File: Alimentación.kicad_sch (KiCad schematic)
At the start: 9 parts, among them J2 Screw_Terminal_01x03, U2 TL074, U3 TL072

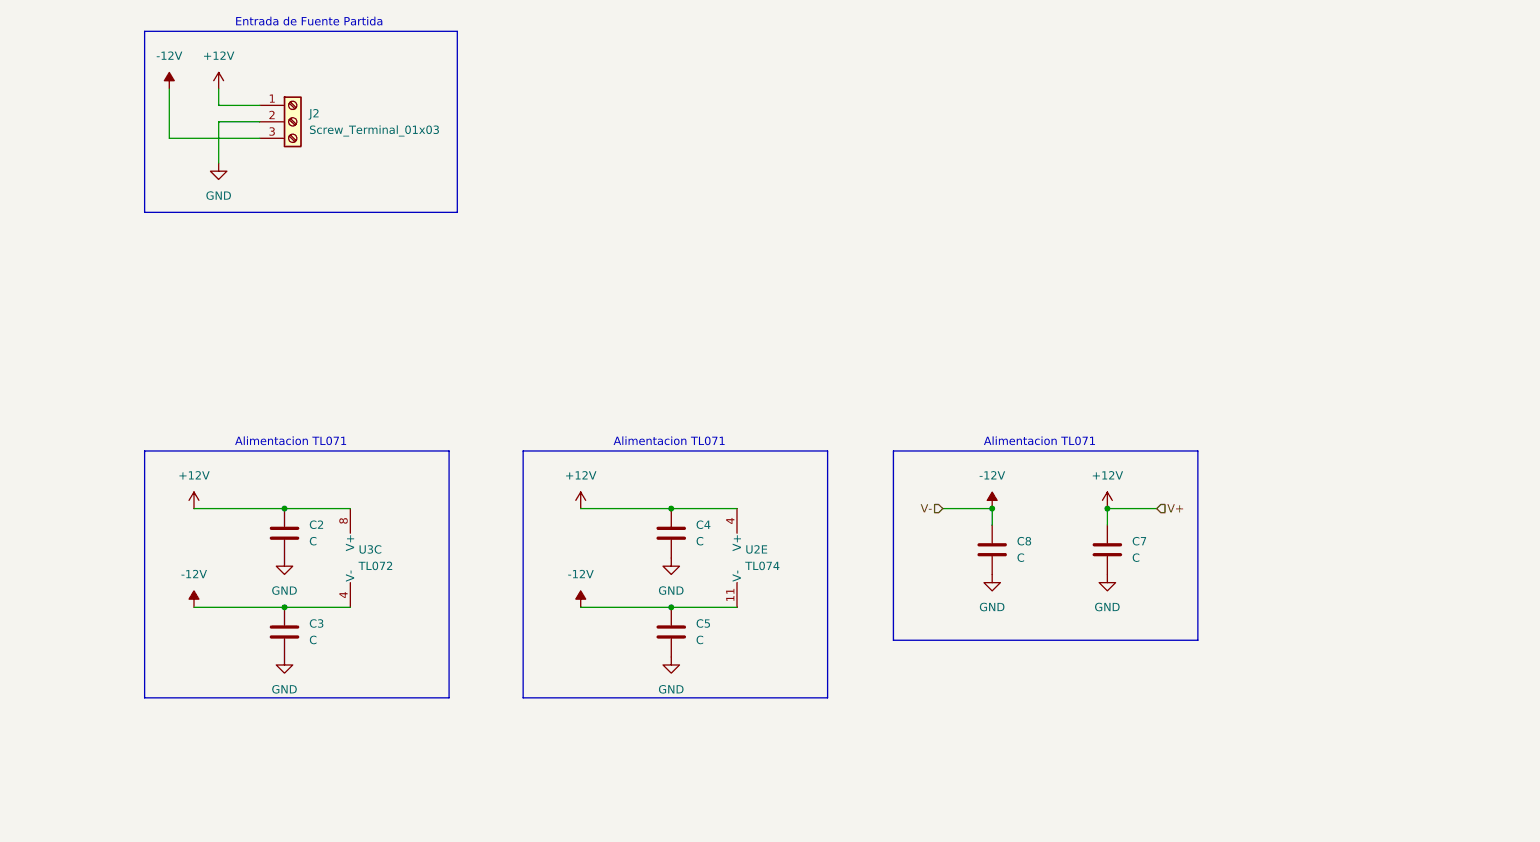
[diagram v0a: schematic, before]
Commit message: Update schematics: signal conditioning, power, ESP32-S3, output, and add signal measurement sub-sheet
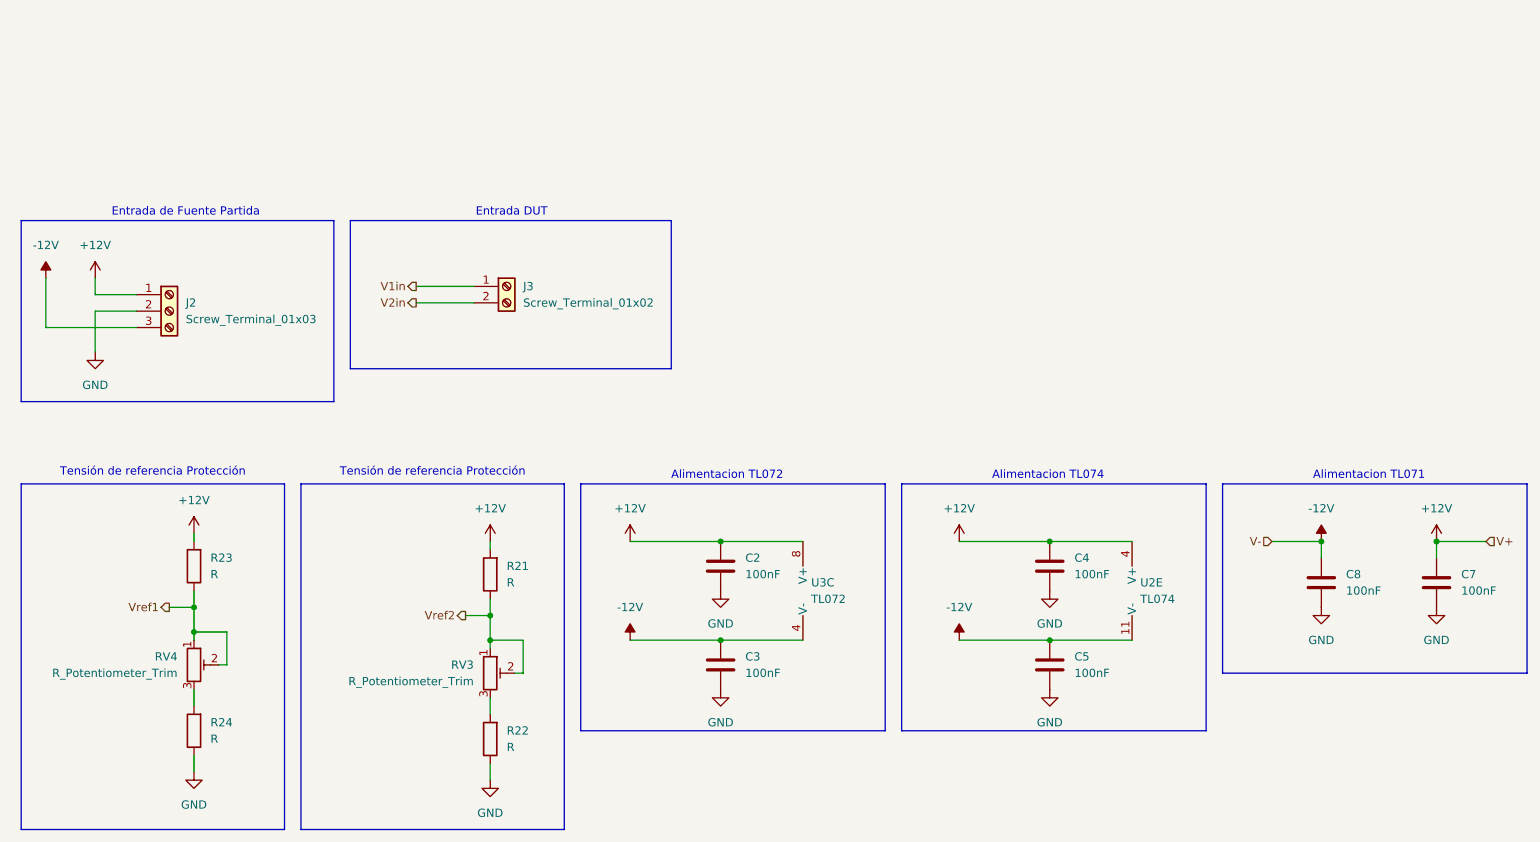
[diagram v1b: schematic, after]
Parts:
- added J3: Screw_Terminal_01x02, TerminalBlock:TerminalBlock_MaiXu_MX126-5.0-02P_1x02_P5.00mm, symbol Connector:Screw_Terminal_01x02
- added R21, R22, R23, R24: R, Resistor_THT:R_Axial_DIN0207_L6.3mm_D2.5mm_P10.16mm_Horizontal, symbol Device:R
- added RV3, RV4: R_Potentiometer_Trim, Potentiometer_THT:Potentiometer_Bourns_3266Y_Vertical, symbol Device:R_Potentiometer_Trim
- C2, C3, C4, C5, C7, C8: value C -> 100nF; footprint (none) -> Capacitor_THT:C_Disc_D7.5mm_W2.5mm_P5.00mm
- J2: footprint (none) -> TerminalBlock:TerminalBlock_MaiXu_MX126-5.0-03P_1x03_P5.00mm
- U2: footprint (none) -> Package_DIP:CERDIP-14_W7.62mm_SideBrazed_LongPads_Socket
- U3: footprint (none) -> Package_DIP:CERDIP-8_W7.62mm_SideBrazed_LongPads_Socket
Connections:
- net +12V: now also R21.2, R23.2
- net GND: now also R22.1, R24.1
- new net: R24.2, RV4.3
- new net: R22.2, RV3.3
- new net V1in: J3.1 (Pin_1)
- new net V2in: J3.2 (Pin_2)
- new net Vref1: R23.1, RV4.1, RV4.2
- new net Vref2: R21.1, RV3.1, RV3.2
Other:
- note added: "Alimentacion TL072"
- note added: "Alimentacion TL074"
- note added: "Entrada DUT"
- note added: "Tensión de referencia Protección"
- moved on the sheet: C2, C3, C4, C5, C7, C8, J2, U2E, U3C
